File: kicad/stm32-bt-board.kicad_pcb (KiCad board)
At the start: 4 copper layers, 0 parts

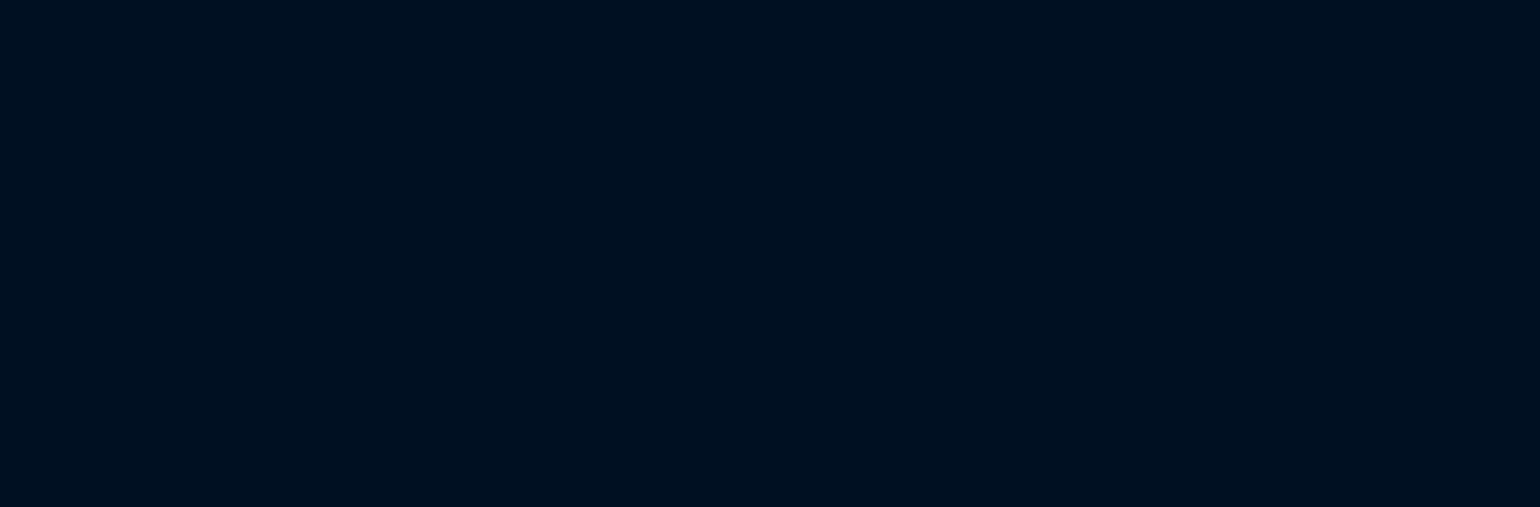
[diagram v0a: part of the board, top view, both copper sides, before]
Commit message: feat(layout): update layout from schematic
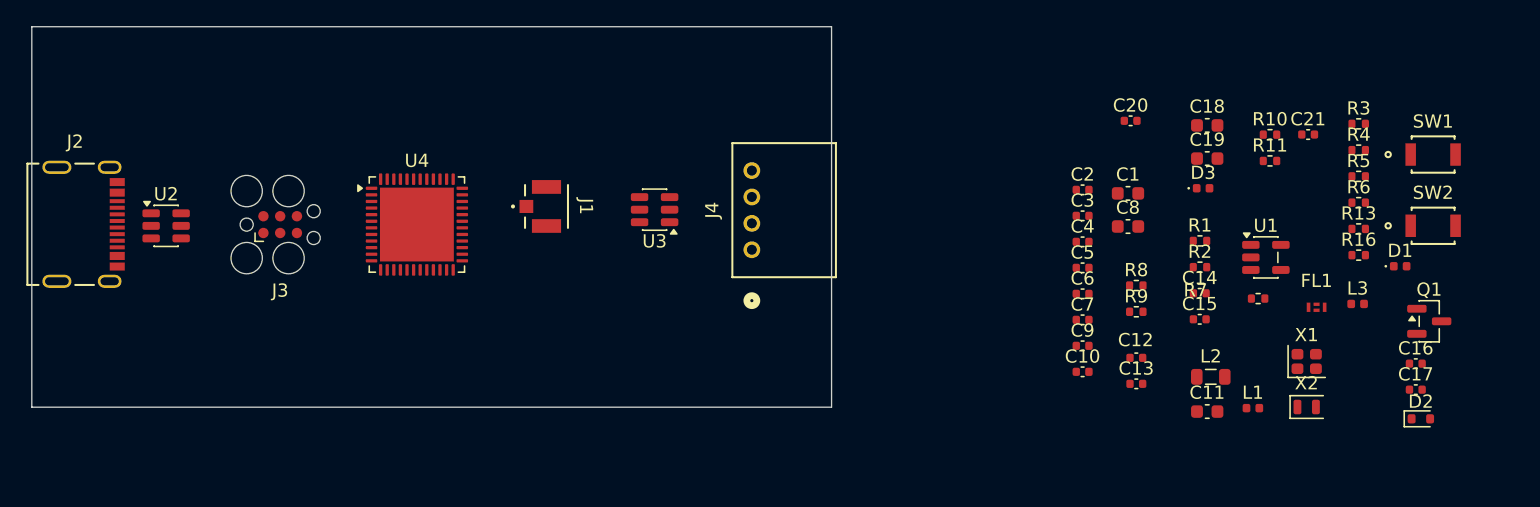
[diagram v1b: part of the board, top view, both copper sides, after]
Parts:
- added C1: 4u7, Capacitor_SMD:C_0603_1608Metric, F.Cu at (182.9, 89.0)
- added C10: 100n, Capacitor_SMD:C_0402_1005Metric, F.Cu at (179.5, 102.5)
- added C11: 4u7, Capacitor_SMD:C_0603_1608Metric, F.Cu at (188.9, 105.5)
- added C12: 0p8, Capacitor_SMD:C_0402_1005Metric, F.Cu at (183.6, 101.4)
- added C13: 0p3, Capacitor_SMD:C_0402_1005Metric, F.Cu at (183.6, 103.4)
- added C14: 10p, Capacitor_SMD:C_0402_1005Metric, F.Cu at (188.4, 96.5)
- added C15: 10p, Capacitor_SMD:C_0402_1005Metric, F.Cu at (188.4, 98.5)
- added C16: 100n, Capacitor_SMD:C_0402_1005Metric, F.Cu at (204.8, 101.9)
- added C17: 100n, Capacitor_SMD:C_0402_1005Metric, F.Cu at (204.8, 103.8)
- added C18: 4u7, Capacitor_SMD:C_0603_1608Metric, F.Cu at (188.9, 83.8)
- added C19: 4u7, Capacitor_SMD:C_0603_1608Metric, F.Cu at (188.9, 86.3)
- added C2: 100n, Capacitor_SMD:C_0402_1005Metric, F.Cu at (179.5, 88.7)
- added C20: 100n, Capacitor_SMD:C_0402_1005Metric, F.Cu at (183.1, 83.5)
- added C21: 100n, Capacitor_SMD:C_0402_1005Metric, F.Cu at (196.6, 84.5)
- added C3: 100n, Capacitor_SMD:C_0402_1005Metric, F.Cu at (179.5, 90.7)
- added C4: 100n, Capacitor_SMD:C_0402_1005Metric, F.Cu at (179.5, 92.6)
- added C5: 100n, Capacitor_SMD:C_0402_1005Metric, F.Cu at (179.5, 94.6)
- added C6: 100n, Capacitor_SMD:C_0402_1005Metric, F.Cu at (179.5, 96.6)
- added C7: 100n, Capacitor_SMD:C_0402_1005Metric, F.Cu at (179.5, 98.5)
- added C8: 4u7, Capacitor_SMD:C_0603_1608Metric, F.Cu at (182.9, 91.5)
- added C9: 100n, Capacitor_SMD:C_0402_1005Metric, F.Cu at (179.5, 100.5)
- added D1: VLMB1500-GS08, LED_SMD:LED_0402_1005Metric, F.Cu at (203.6, 94.5)
- added D2: BAT54K, Diode_SMD:D_SOD-523, F.Cu at (205.1, 106.0)
- added D3: VLMS1500-GS08, LED_SMD:LED_0402_1005Metric, F.Cu at (188.6, 88.6)
- added FL1: DLF162500LT-5028A1, #stm32-bt-board-external-footprints:DLF162500LT-5028A1, F.Cu at (197.2, 97.6)
- added J1: 1909763-1, #stm32-bt-board-external-footprints:1909763-1, F.Cu at (138.9, 90.0)
- added J2: 2171790001, #stm32-bt-board-external-footprints:2171790001, F.Cu at (103.0, 91.3)
- added J3: Conn_ARM_SWD_TagConnect_TC2030, Connector:Tag-Connect_TC2030-IDC-FP_2x03_P1.27mm_Vertical, F.Cu at (118.7, 91.3)
- added J4: S4B-PH-K-S(LF)(SN), #stm32-bt-board-external-footprints:S4B-PH-K-S(LF)(SN), F.Cu at (154.4, 93.2)
- added L1: 10n, Inductor_SMD:L_0402_1005Metric, F.Cu at (192.4, 105.2)
- added L2: 10u, Inductor_SMD:L_0805_2012Metric, F.Cu at (189.2, 102.9)
- added L3: 2n7, Inductor_SMD:L_0402_1005Metric, F.Cu at (200.3, 97.3)
- added Q1: S9013-E, Package_TO_SOT_SMD:SOT-23, F.Cu at (205.8, 98.7)
- added R1: 0R, Resistor_SMD:R_0402_1005Metric, F.Cu at (188.4, 92.6)
- added R10: 220R, Resistor_SMD:R_0402_1005Metric, F.Cu at (193.7, 84.5)
- added R11: 220R, Resistor_SMD:R_0402_1005Metric, F.Cu at (193.7, 86.5)
- added R13: 5k1, Resistor_SMD:R_0402_1005Metric, F.Cu at (200.4, 91.7)
- added R16: 5k1, Resistor_SMD:R_0402_1005Metric, F.Cu at (200.4, 93.7)
- added R2: 0R, Resistor_SMD:R_0402_1005Metric, F.Cu at (188.4, 94.6)
- added R3: 0R, Resistor_SMD:R_0402_1005Metric, F.Cu at (200.4, 83.7)
- added R4: 220R, Resistor_SMD:R_0402_1005Metric, F.Cu at (200.4, 85.7)
- added R5: 5k1, Resistor_SMD:R_0402_1005Metric, F.Cu at (200.4, 87.7)
- added R6: 100k, Resistor_SMD:R_0402_1005Metric, F.Cu at (200.4, 89.7)
- added R7: 220R, Resistor_SMD:R_0402_1005Metric, F.Cu at (192.8, 96.9)
- added R8: 5k1, Resistor_SMD:R_0402_1005Metric, F.Cu at (183.6, 96.0)
- added R9: 5k1, Resistor_SMD:R_0402_1005Metric, F.Cu at (183.6, 97.9)
- added SW1: B3U-1000P, #stm32-bt-board-external-footprints:B3U-1000P, F.Cu at (206.1, 86.0)
- added SW2: B3U-1000P, #stm32-bt-board-external-footprints:B3U-1000P, F.Cu at (206.1, 91.4)
- added U1: MIC5365-3.3YD5, Package_TO_SOT_SMD:TSOT-23-5, F.Cu at (193.4, 93.8)
- added U2: USBLC6-2SC6, Package_TO_SOT_SMD:SOT-23-6, F.Cu at (110.1, 91.4)
- added U3: USBLC6-2SC6, Package_TO_SOT_SMD:SOT-23-6, F.Cu at (147.1, 90.2)
- added U4: STM32WB55CEU6, Package_DFN_QFN:QFN-48-1EP_7x7mm_P0.5mm_EP5.6x5.6mm, F.Cu at (129.1, 91.3)
- added X1: 32MHz, Crystal:Crystal_SMD_2016-4Pin_2.0x1.6mm, F.Cu at (196.5, 101.7)
- added X2: 32kHz768, Crystal:Crystal_SMD_2012-2Pin_2.0x1.2mm, F.Cu at (196.5, 105.2)
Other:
- board outline added: 60.6 x 28.8 mm

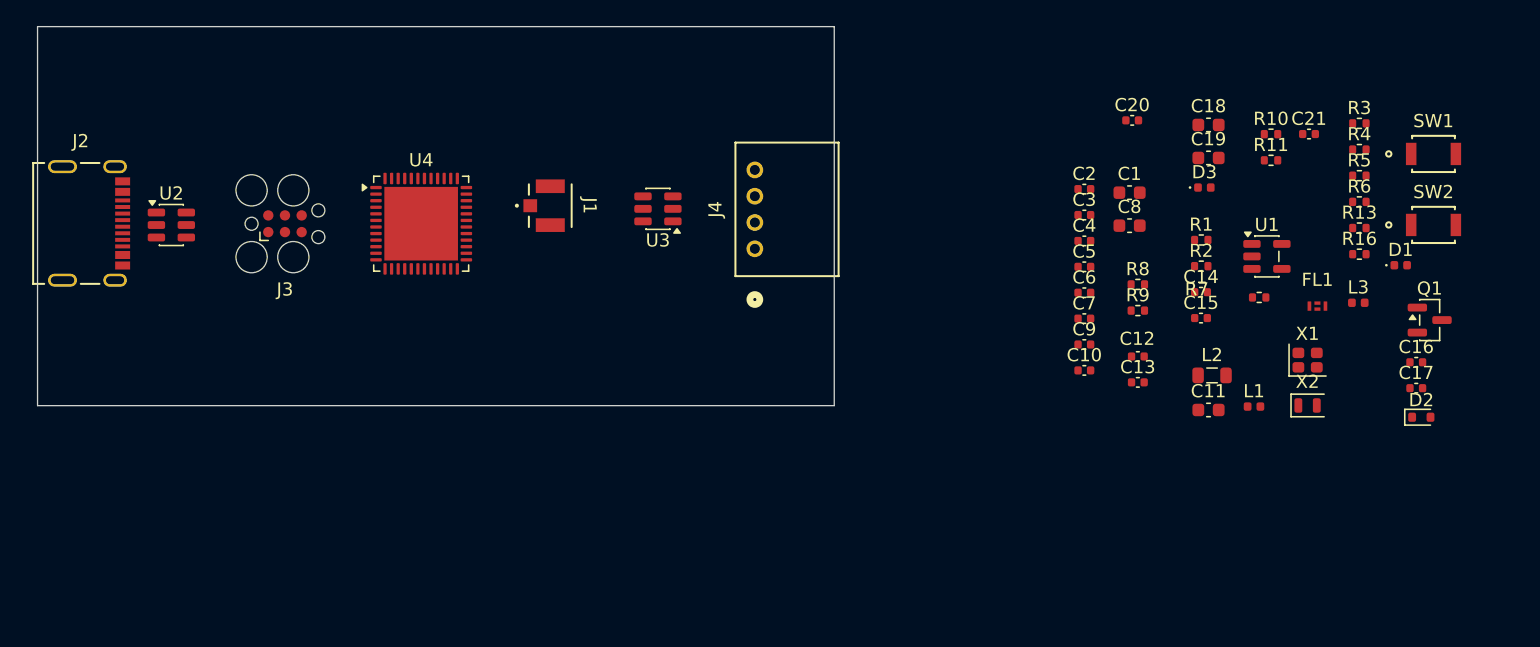
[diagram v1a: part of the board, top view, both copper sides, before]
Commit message: feat(layout): start a rough layout with netclasses
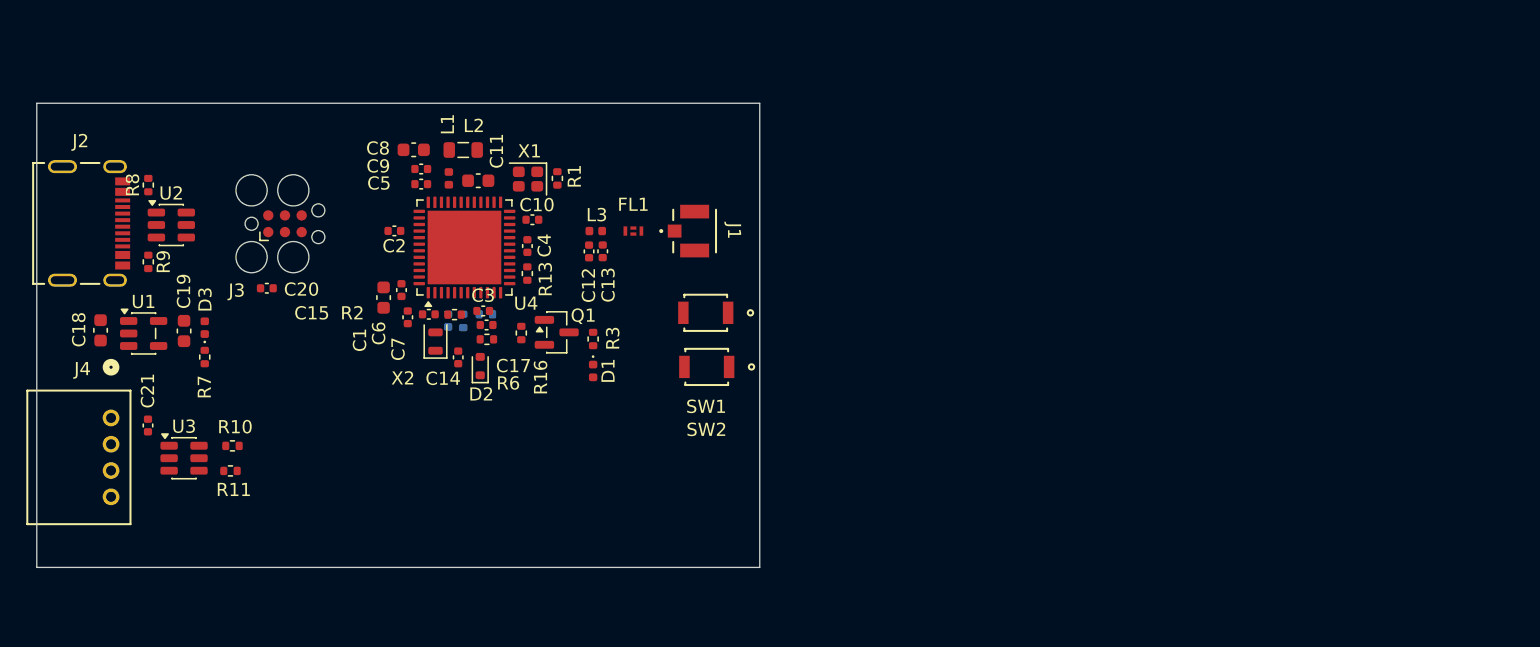
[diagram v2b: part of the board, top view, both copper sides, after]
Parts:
- C16, R4, R5: moved to B.Cu
- moved C21 91.1 mm to (108.3, 106.7), turned to -90 degrees
- moved C18 85.7 mm to (104.7, 99.4), turned to -90 degrees
- moved U1 85.6 mm to (108.0, 99.7)
- moved R11 82.6 mm to (114.6, 110.1)
- moved R10 82.5 mm to (114.7, 108.2)
- moved R7 80.3 mm to (112.6, 101.5), turned to -90 degrees
- moved C19 79.0 mm to (111.0, 99.5), turned to -90 degrees
- moved D3 76.8 mm to (112.6, 99.2), turned to 90 degrees
- moved R8 75.6 mm to (108.3, 88.4), turned to 90 degrees
- moved R9 75.4 mm to (108.3, 94.2), turned to -90 degrees
- moved C16 73.7 mm to (131.1, 98.7), turned to -90 degrees
- moved D2 71.7 mm to (133.6, 102.2), turned to 90 degrees
- moved C17 70.9 mm to (134.0, 99.0)
- moved R5 69.1 mm to (132.3, 98.7), turned to -90 degrees
- moved R4 67.6 mm to (134.0, 98.2)
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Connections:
- net Net-(C14-Pad1) renamed /Microcontroller/Crystals/LSE_IN_R
- SW1 pad 1: Net-(R4-Pad1) -> +3V3
- SW1 pad 2: +3V3 -> Net-(R4-Pad1)
- U3 pad 5: +5V -> +3V3
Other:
- board size 60.6 x 28.8 mm -> 55 x 35.3 mm

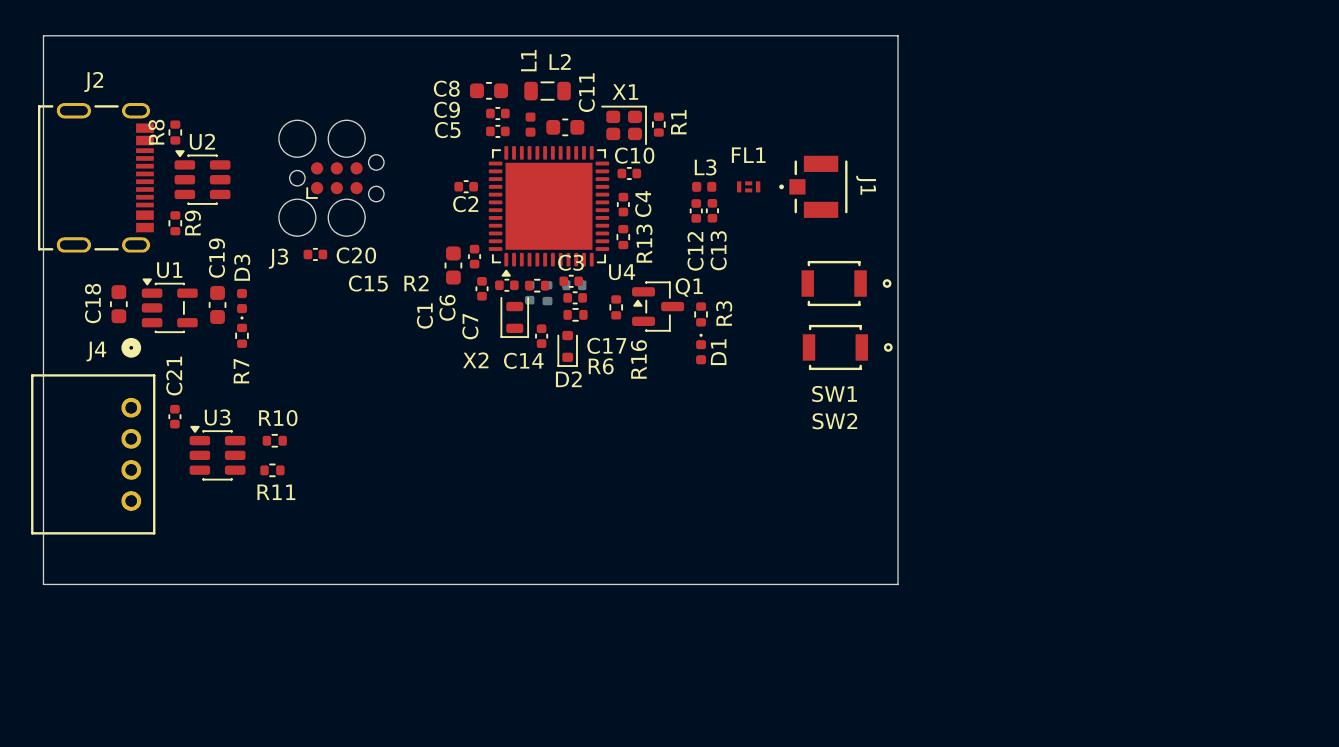
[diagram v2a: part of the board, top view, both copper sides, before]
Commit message: refactor(layout): miscellaneous edits
move components
add github profile link
add silkscreen for the 2 buttons; user and boot0
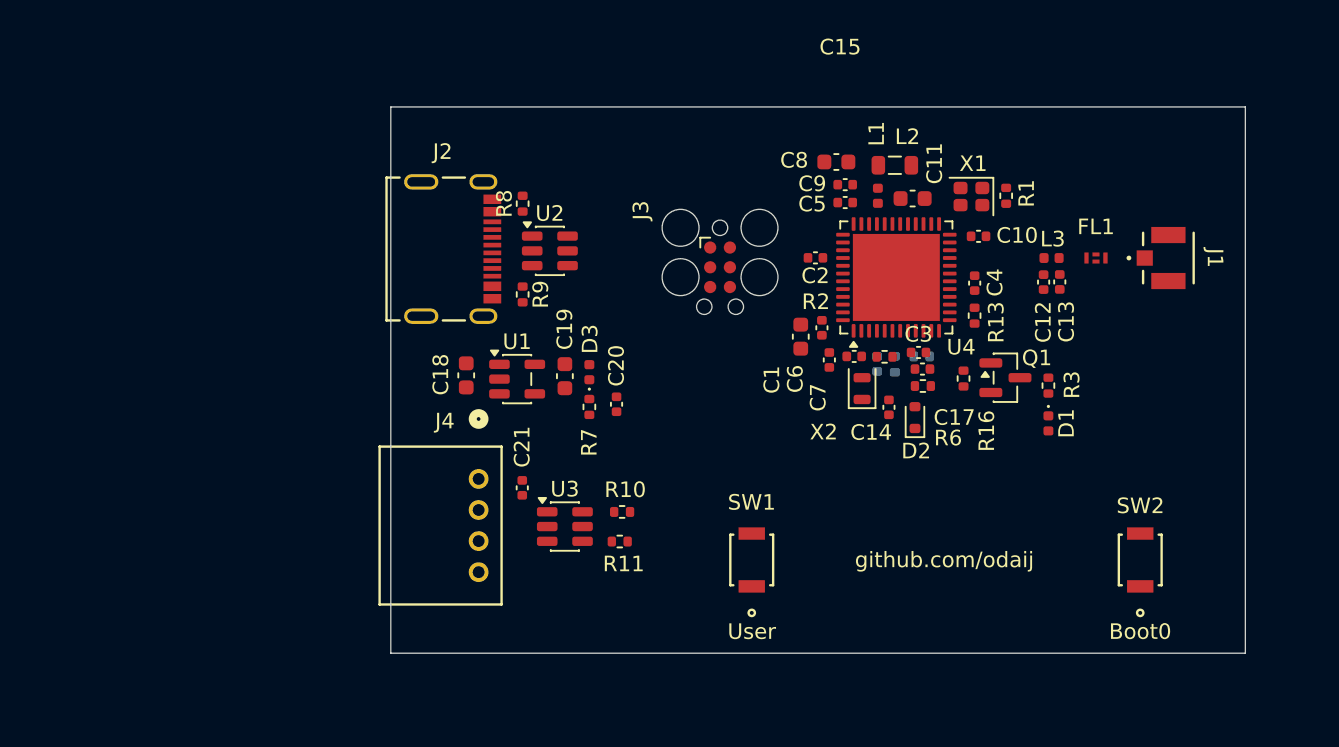
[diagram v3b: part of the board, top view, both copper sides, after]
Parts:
- moved J3 25.3 mm to (143.4, 97.1), turned to -90 degrees
- moved SW2 23.9 mm to (170.4, 115.9), turned to 90 degrees
- moved C4 23.2 mm to (159.7, 98.1)
- moved R13 23.2 mm to (159.7, 100.2)
- moved C2 22.9 mm to (149.5, 96.5)
- moved L2 22.9 mm to (154.6, 90.5)
- moved C10 22.8 mm to (160.0, 95.1)
- moved C19 22.8 mm to (133.4, 104.1)
- moved C21 22.8 mm to (130.6, 111.3)
- moved U3 22.8 mm to (133.4, 113.7)
- moved C5 22.8 mm to (151.4, 92.9)
- moved C6 22.8 mm to (149.9, 101.0)
- moved C8 22.8 mm to (150.8, 90.3)
- moved R1 22.8 mm to (161.8, 92.5)
- moved R16 22.8 mm to (159.0, 104.2)
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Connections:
- net /Microcontroller/Crystals/LSE_IN_R renamed /Microcontroller/Crystals/OSC_LSE_OUT_R
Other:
- board size 55 x 35.3 mm -> 55 x 35.2 mm
- board text added: "Boot0"
- board text added: "User"
- board text added: "github.com/odaij"
